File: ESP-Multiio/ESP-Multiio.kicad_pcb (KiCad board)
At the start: 2 copper layers, 75 x 59 mm, 50 parts, among them J1 Conn_01x10, Q1 BC337, SW1 SW_SPDT_MSM, SW2 SW_SPDT_MSM, SW3 SW_SPDT_MSM, SW4 SW_SPDT_MSM, U1 WeMos_D1_mini, U2 MCP23017_SP, U4 TSOP1838

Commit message: more 3.3V fill
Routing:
- net /GPB6: track 100.9 -> 102.7 mm
- net /GPB4: track 94.2 -> 96.0 mm
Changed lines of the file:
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@@
     (thickness 1.6)
     (drawings 51)
-    (tracks 363)
+    (tracks 367)
     (zones 0)
     (modules 50)
@@
     (add_net "Net-(Q1-Pad1)")
     (add_net "Net-(Q1-Pad2)")
-    (add_net "Net-(U2-Pad11)")
-    (add_net "Net-(U2-Pad14)")
     (add_net SCL)
     (add_net SDA)
@@
   (segment (start 80.7 51.8) (end 80.7 51.05) (width 0.25) (layer B.Cu) (net 42))
   (segment (start 82.77501 53.87501) (end 80.7 51.8) (width 0.25) (layer B.Cu) (net 42))
-  (segment (start 92.424972 75.234892) (end 92.424972 60.690465) (width 0.25) (layer B.Cu) (net 42))
+  (segment (start 87.87501 53.87501) (end 85.12499 53.87501) (width 0.25) (layer B.Cu) (net 42))
+  (segment (start 92.424972 75.234892) (end 92.424972 58.424972) (width 0.25) (layer B.Cu) (net 42))
+  (segment (start 92.424972 58.424972) (end 87.87501 53.87501) (width 0.25) (layer B.Cu) (net 42))
   (segment (start 96.19013 79.00005) (end 92.424972 75.234892) (width 0.25) (layer B.Cu) (net 42))
-  (segment (start 112.61259 75.80874) (end 109.42128 79.00005) (width 0.25) (layer B.Cu) (net 42))
+  (segment (start 109.42128 79.00005) (end 96.19013 79.00005) (width 0.25) (layer B.Cu) (net 42))
+  (segment (start 112.61259 68.836406) (end 112.61259 75.80874) (width 0.25) (layer B.Cu) (net 42))
+  (segment (start 85.12499 53.87501) (end 82.77501 53.87501) (width 0.25) (layer B.Cu) (net 42))
+  (segment (start 85.609517 53.87501) (end 85.12499 53.87501) (width 0.25) (layer B.Cu) (net 42))
+  (segment (start 118.065994 64.42501) (end 117.023986 64.42501) (width 0.25) (layer B.Cu) (net 42))
   (segment (start 135.84 45.62) (end 135.040001 46.419999) (width 0.25) (layer B.Cu) (net 42))
+  (segment (start 112.61259 75.80874) (end 109.42128 79.00005) (width 0.25) (layer B.Cu) (net 42))
   (segment (start 135.040001 46.419999) (end 135.040001 47.451003) (width 0.25) (layer B.Cu) (net 42))
-  (segment (start 85.609517 53.87501) (end 82.77501 53.87501) (width 0.25) (layer B.Cu) (net 42))
-  (segment (start 135.040001 47.451003) (end 118.065994 64.42501) (width 0.25) (layer B.Cu) (net 42))
   (segment (start 117.023986 64.42501) (end 112.61259 68.836406) (width 0.25) (layer B.Cu) (net 42))
-  (segment (start 92.424972 60.690465) (end 85.609517 53.87501) (width 0.25) (layer B.Cu) (net 42))
-  (segment (start 118.065994 64.42501) (end 117.023986 64.42501) (width 0.25) (layer B.Cu) (net 42))
-  (segment (start 109.42128 79.00005) (end 96.19013 79.00005) (width 0.25) (layer B.Cu) (net 42))
-  (segment (start 112.61259 68.836406) (end 112.61259 75.80874) (width 0.25) (layer B.Cu) (net 42))
+  (segment (start 135.040001 47.451003) (end 118.065994 64.42501) (width 0.25) (layer B.Cu) (net 42))
   (segment (start 92.874981 75.048491) (end 92.874981 56.124981) (width 0.25) (layer B.Cu) (net 43))
   (segment (start 92.874981 56.124981) (end 90 53.25) (width 0.25) (layer B.Cu) (net 43))
@@
   (segment (start 112.16258 66.746416) (end 117.023986 61.88501) (width 0.25) (layer B.Cu) (net 43))
   (segment (start 82.77501 42.87501) (end 80.7 40.8) (width 0.25) (layer B.Cu) (net 44))
-  (segment (start 93.32499 50.590483) (end 85.609517 42.87501) (width 0.25) (layer B.Cu) (net 44))
-  (segment (start 96.56293 78.10003) (end 93.32499 74.86209) (width 0.25) (layer B.Cu) (net 44))
-  (segment (start 93.32499 74.86209) (end 93.32499 50.590483) (width 0.25) (layer B.Cu) (net 44))
+  (segment (start 80.7 40.8) (end 80.7 40.05) (width 0.25) (layer B.Cu) (net 44))
+  (segment (start 87.87501 42.87501) (end 85.12499 42.87501) (width 0.25) (layer B.Cu) (net 44))
+  (segment (start 93.32499 74.86209) (end 93.32499 48.32499) (width 0.25) (layer B.Cu) (net 44))
   (segment (start 109.04848 78.10003) (end 96.56293 78.10003) (width 0.25) (layer B.Cu) (net 44))
+  (segment (start 111.71257 64.656426) (end 111.71257 75.43594) (width 0.25) (layer B.Cu) (net 44))
+  (segment (start 117.023986 59.34501) (end 111.71257 64.656426) (width 0.25) (layer B.Cu) (net 44))
+  (segment (start 85.12499 42.87501) (end 82.77501 42.87501) (width 0.25) (layer B.Cu) (net 44))
+  (segment (start 118.065994 59.34501) (end 117.023986 59.34501) (width 0.25) (layer B.Cu) (net 44))
+  (segment (start 96.56293 78.10003) (end 93.32499 74.86209) (width 0.25) (layer B.Cu) (net 44))
+  (segment (start 129.960001 46.419999) (end 129.960001 47.451003) (width 0.25) (layer B.Cu) (net 44))
+  (segment (start 85.609517 42.87501) (end 85.12499 42.87501) (width 0.25) (layer B.Cu) (net 44))
   (segment (start 111.71257 75.43594) (end 109.04848 78.10003) (width 0.25) (layer B.Cu) (net 44))
   (segment (start 130.76 45.62) (end 129.960001 46.419999) (width 0.25) (layer B.Cu) (net 44))
+  (segment (start 93.32499 48.32499) (end 87.87501 42.87501) (width 0.25) (layer B.Cu) (net 44))
   (segment (start 129.960001 47.451003) (end 118.065994 59.34501) (width 0.25) (layer B.Cu) (net 44))
-  (segment (start 80.7 40.8) (end 80.7 40.05) (width 0.25) (layer B.Cu) (net 44))
-  (segment (start 129.960001 46.419999) (end 129.960001 47.451003) (width 0.25) (layer B.Cu) (net 44))
-  (segment (start 111.71257 64.656426) (end 111.71257 75.43594) (width 0.25) (layer B.Cu) (net 44))
-  (segment (start 85.609517 42.87501) (end 82.77501 42.87501) (width 0.25) (layer B.Cu) (net 44))
-  (segment (start 118.065994 59.34501) (end 117.023986 59.34501) (width 0.25) (layer B.Cu) (net 44))
-  (segment (start 117.023986 59.34501) (end 111.71257 64.656426) (width 0.25) (layer B.Cu) (net 44))
   (segment (start 90.1 40.8) (end 90.1 40.05) (width 0.25) (layer B.Cu) (net 45))
   (segment (start 93.774999 44.474999) (end 90.1 40.8) (width 0.25) (layer B.Cu) (net 45))

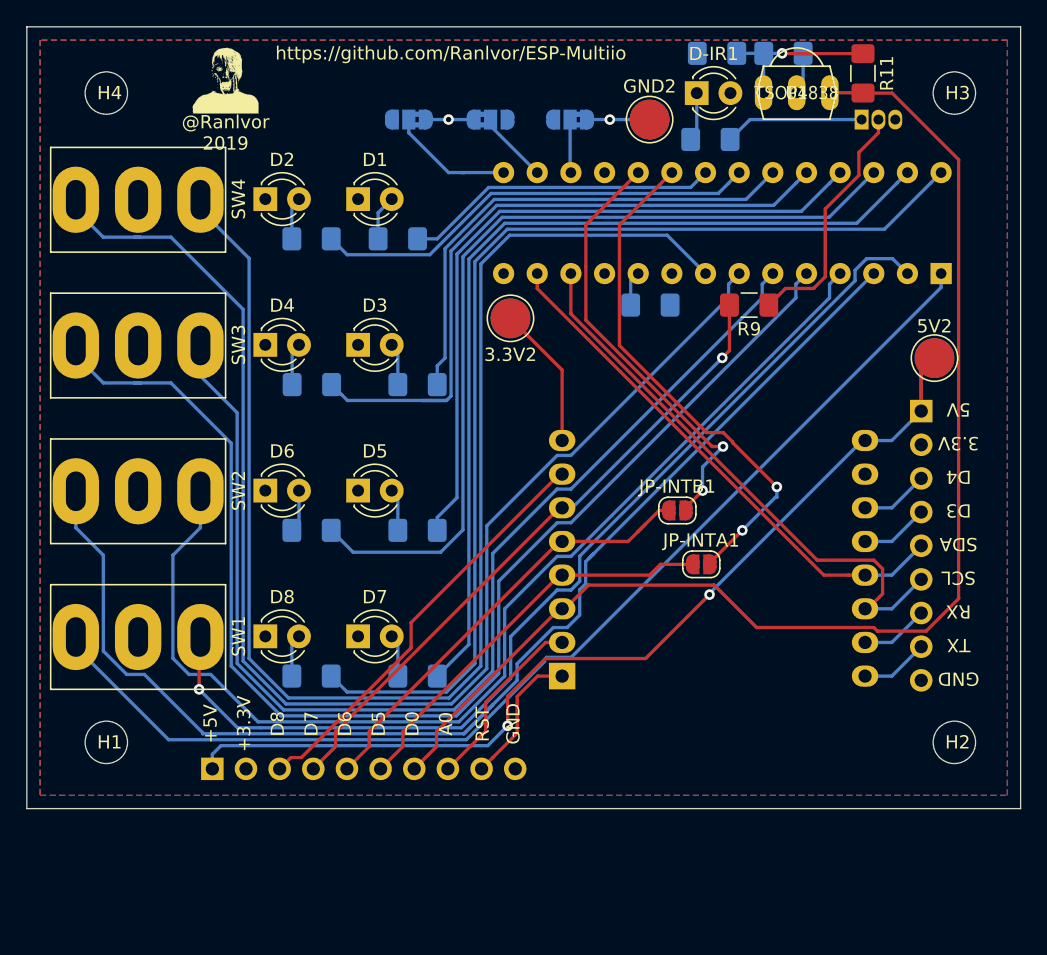
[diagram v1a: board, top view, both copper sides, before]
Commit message: Change board dimensions
Because the switches need to be further appart
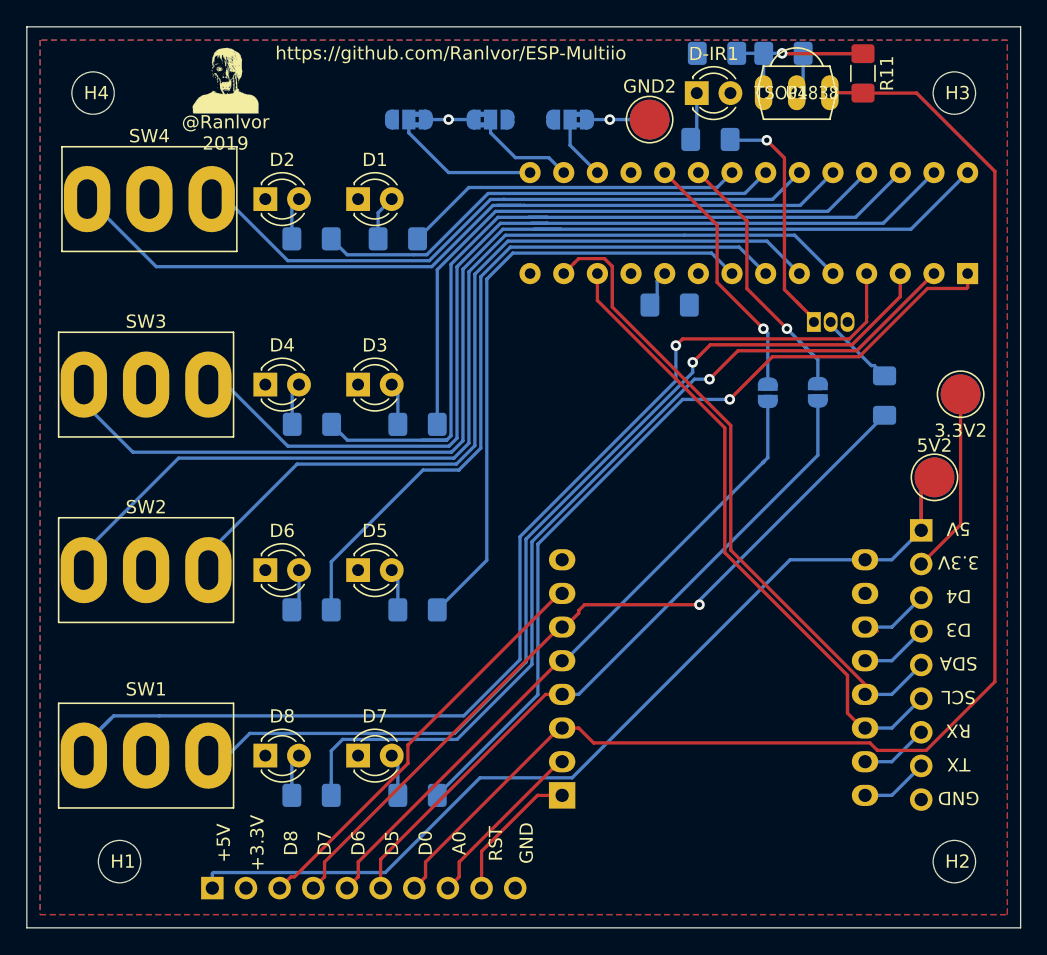
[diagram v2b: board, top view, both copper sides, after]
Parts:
- JP-INTA1, JP-INTB1, R9: moved to B.Cu
- moved 3.3V1 34.5 mm to (147.5, 54.7)
- moved 3.3V2 34.5 mm to (147.5, 54.7)
- moved Q1 15.7 mm to (136.4, 49.3)
- moved JP-INTA1 15.7 mm to (136.7, 54.6), turned to 90 degrees
- moved R9 12.3 mm to (141.7, 54.8), turned to 270 degrees
- moved JP-INTB1 11.2 mm to (132.9, 54.6), turned to 90 degrees
- moved H1 9.06 mm to (84.0, 90.0)
- moved 5V1 9.00 mm to (145.5, 61.0)
- moved 5V2 9.00 mm to (145.5, 61.0)
- moved D7 9.00 mm to (102.0, 82.0)
- moved D8 9.00 mm to (95.0, 82.0)
- moved H2 9.00 mm to (147.0, 90.0)
- moved I2C1 9.00 mm to (144.5, 65.0)
- moved J1 9.00 mm to (91.0, 92.0)
- moved R7 9.00 mm to (106.5, 85.0)
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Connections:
- R3 pad 2: /GPA2 -> /GPA4
- R4 pad 2: /GPA3 -> /GPA5
- R5 pad 2: /GPA4 -> /GPB7
- R6 pad 2: /GPA5 -> /GPB6
- R7 pad 2: /GPA6 -> /GPB0
- R8 pad 2: /GPA7 -> /GPB1
- SW1 pad 1: /GPB1 -> /GPB2
- SW1 pad 3: /GPB0 -> /GPB3
- SW2 pad 1: /GPB3 -> /GPB5
- SW2 pad 3: /GPB2 -> /GPB4
- SW3 pad 1: /GPB5 -> /GPA6
- SW3 pad 3: /GPB4 -> /GPA7
- SW4 pad 1: /GPB7 -> /GPA2
- SW4 pad 3: /GPB6 -> /GPA3
- U2 pad 11: (no net) -> Net-(U2-Pad11)
- U2 pad 14: (no net) -> Net-(U2-Pad14)
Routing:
- net /GPB7: track 105.3 -> 46.5 mm
- net /GPB6: track 102.7 -> 54.7 mm
- net /D5: track 30.6 -> 51.9 mm
- net /GPB0: track 84.2 -> 63.6 mm, vias 0 -> 1
- net /GPB5: track 84.3 -> 64.5 mm
- net /GPB4: track 96.0 -> 76.8 mm
- net Net-(JP-INTA1-Pad2): track 39.0 -> 21.3 mm, vias 2 -> 1
- net /GPB2: track 94.5 -> 77.6 mm, vias 0 -> 1
- net /D6: track 33.9 -> 50.3 mm
- net Net-(JP-INTB1-Pad2): track 33.1 -> 19.3 mm, vias 2 -> 1
- net /GPA3: track 51.7 -> 64.7 mm
- net Net-(Q1-Pad2): track 18.7 -> 5.88 mm
- net /GPA2: track 37.6 -> 49.9 mm
- net /D0: track 95.4 -> 106.6 mm
- net /D7: track 48.6 -> 58.9 mm
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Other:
- board size 75 x 59 mm -> 75 x 68 mm

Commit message: Mechanical Details, Mechanical data in Silkscreen
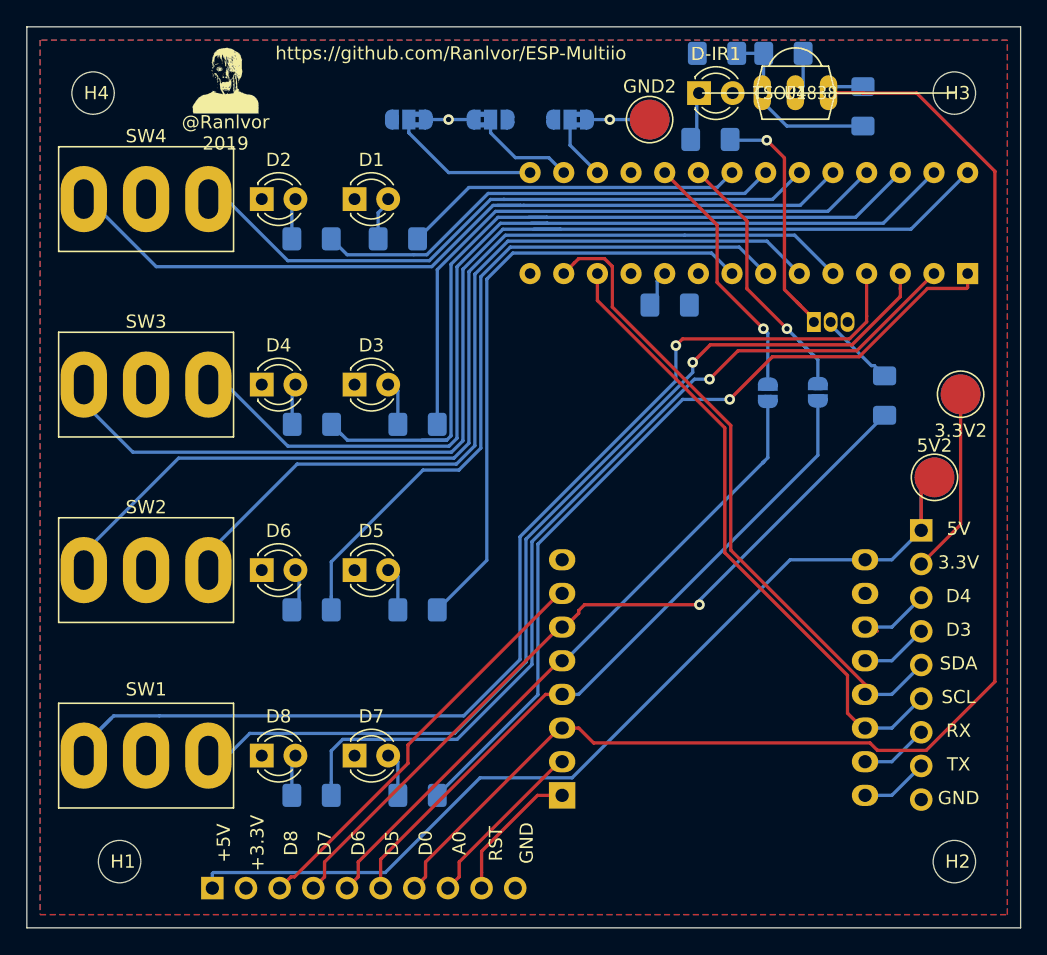
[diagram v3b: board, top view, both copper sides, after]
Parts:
- R11: moved to B.Cu
- moved R11 2.49 mm to (140.1, 33.0), turned to 90 degrees
- moved D1 0.27 mm to (101.7, 40.0)
- moved D2 0.27 mm to (94.7, 40.0)
- moved D3 0.27 mm to (101.7, 54.0)
- moved D4 0.27 mm to (94.7, 54.0)
- moved D5 0.27 mm to (101.7, 68.0)
- moved D6 0.27 mm to (94.7, 68.0)
- moved D7 0.27 mm to (101.7, 82.0)
- moved D8 0.27 mm to (94.7, 82.0)
- moved SW4 0.25 mm to (86.0, 40.0)
- moved D-IR1 0.17 mm to (127.7, 32.0)
- moved U4 0.10 mm to (135.0, 32.0)
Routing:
- net /D0: track 106.6 -> 109.4 mm
- net Net-(C2-Pad1): track 13.2 -> 14.7 mm, vias 1 -> 0

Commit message: More fill
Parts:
- moved 5V1 0.50 mm to (145.0, 61.0)
- moved 5V2 0.50 mm to (145.0, 61.0)
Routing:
- net /GPB3: track 86.6 -> 83.7 mm
- net /GPA6: track 74.6 -> 76.5 mm
- net /GPA2: track 49.9 -> 51.8 mm
- net /GPB1: track 69.2 -> 69.7 mm
